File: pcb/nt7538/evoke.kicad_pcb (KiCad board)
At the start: 2 copper layers, 60 x 45 mm, 42 parts, among them J1 Conn_01x03_Male, J2 BACKLIGHT_CONN, J3 SUPP_PWR, Q1 Q_NMOS_GSD, U1 STM32F103C8Tx

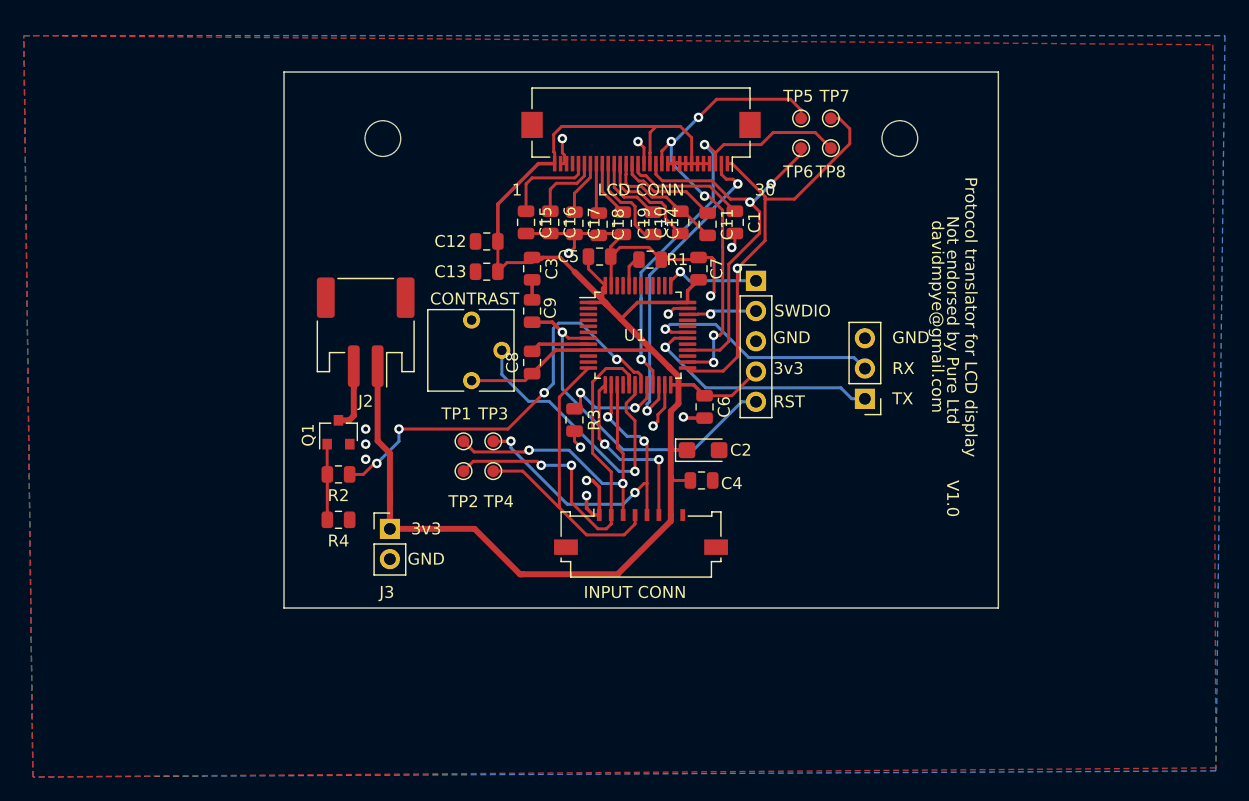
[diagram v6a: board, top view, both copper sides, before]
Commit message: Move screw holes for the nt7538 PCB, and increment PCB version number to 1.1
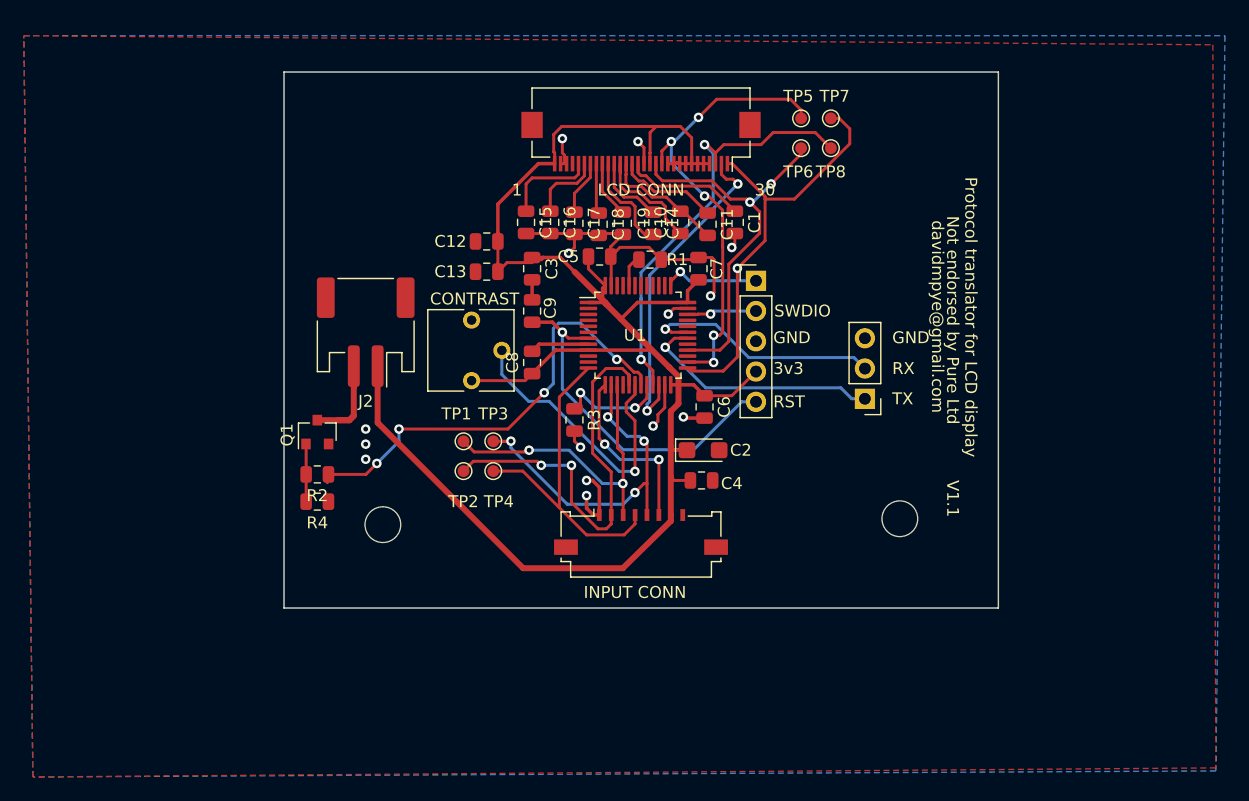
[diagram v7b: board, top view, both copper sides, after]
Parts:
- removed J3: SUPP_PWR, Connector_PinHeader_2.54mm:PinHeader_1x02_P2.54mm_Vertical
- moved REF** 32.4 mm to (83.2, 69.5)
- moved REF** 31.9 mm to (126.6, 69.0)
- moved R4 2.34 mm to (77.7, 67.6)
- moved Q1 1.78 mm to (77.7, 61.7)
- moved R2 1.78 mm to (77.7, 65.3)
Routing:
- net +3V3: track 157.2 -> 151.0 mm
- net Net-(J2-Pad2): track 5.61 -> 8.83 mm
- net LCD_BACKLIGHT_PWM: track 35.7 -> 38.4 mm
- net Net-(Q1-Pad1): track 7.06 -> 4.85 mm
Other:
- board text added: "V1.1"
- board text removed: "V1.0"
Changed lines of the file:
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@@
   (general
     (thickness 1.6)
-    (drawings 19)
-    (tracks 474)
+    (drawings 17)
+    (tracks 467)
     (zones 0)
-    (modules 42)
+    (modules 41)
     (nets 57)
   )
@@
   )
   (module MountingHole:MountingHole_3mm locked (layer F.Cu)
-    (at 126.63 37.084)
+    (at 126.63 69)
     (descr "Mounting Hole 3mm, no annular")
     (tags "mounting hole 3mm no annular")
@@
   )
   (module MountingHole:MountingHole_3mm locked (layer F.Cu)
-    (at 83.23 37.084)
+    (at 83.23 69.496)
     (descr "Mounting Hole 3mm, no annular")
     (tags "mounting hole 3mm no annular")
@@
   )
   (module Package_TO_SOT_SMD:SOT-23 (layer F.Cu)
-    (at 79.502 61.738 90)
+    (at 77.724 61.722 90)
     (descr "SOT-23, Standard")
     (tags SOT-23)
@@
   )
   (module Resistor_SMD:R_0805_2012Metric (layer F.Cu)
-    (at 79.502 65.278)
+    (at 77.724 65.278)
     (descr "Resistor SMD 0805 (2012 Metric), square (rectangular) end terminal, IPC_7351 nominal, (Body size source: https://docs.google.com/spreadsheets/d/1BsfQQcO9C6DZCsRaXUlFlo91Tg2WpOkGARC1WS5S8t0/edit?usp=sharing), generated with kicad-footprint-generator")
     (tags resistor)
@@
   )
   (module Resistor_SMD:R_0805_2012Metric (layer F.Cu)
-    (at 79.502 69.088)
+    (at 77.724 67.564)
     (descr "Resistor SMD 0805 (2012 Metric), square (rectangular) end terminal, IPC_7351 nominal, (Body size source: https://docs.google.com/spreadsheets/d/1BsfQQcO9C6DZCsRaXUlFlo91Tg2WpOkGARC1WS5S8t0/edit?usp=sharing), generated with kicad-footprint-generator")
     (tags resistor)
@@
       (net 53 "Net-(Q1-Pad1)"))
     (model ${KISYS3DMOD}/Resistor_SMD.3dshapes/R_0805_2012Metric.wrl
-      (at (xyz 0 0 0))
-      (scale (xyz 1 1 1))
-      (rotate (xyz 0 0 0))
-    )
-  )
-  (module Connector_PinHeader_2.54mm:PinHeader_1x02_P2.54mm_Vertical (layer F.Cu)
-    (at 83.82 69.85)
-    (descr "Through hole straight pin header, 1x02, 2.54mm pitch, single row")
-    (tags "Through hole pin header THT 1x02 2.54mm single row")
-    (fp_text reference J3 (at -0.254 5.334) (layer F.SilkS)
-      (effects (font (size 1 1) (thickness 0.15)))
-    )
-    (fp_text value SUPP_PWR (at 0 4.87) (layer F.Fab)
-      (effects (font (size 1 1) (thickness 0.15)))
-    )
-    (fp_line (start -0.635 -1.27) (end 1.27 -1.27) (layer F.Fab) (width 0.1))
-    (fp_line (start 1.27 -1.27) (end 1.27 3.81) (layer F.Fab) (width 0.1))
-    (fp_line (start 1.27 3.81) (end -1.27 3.81) (layer F.Fab) (width 0.1))
-    (fp_line (start -1.27 3.81) (end -1.27 -0.635) (layer F.Fab) (width 0.1))
-    (fp_line (start -1.27 -0.635) (end -0.635 -1.27) (layer F.Fab) (width 0.1))
-    (fp_line (start -1.33 3.87) (end 1.33 3.87) (layer F.SilkS) (width 0.12))
-    (fp_line (start -1.33 1.27) (end -1.33 3.87) (layer F.SilkS) (width 0.12))
-    (fp_line (start 1.33 1.27) (end 1.33 3.87) (layer F.SilkS) (width 0.12))
-    (fp_line (start -1.33 1.27) (end 1.33 1.27) (layer F.SilkS) (width 0.12))
-    (fp_line (start -1.33 0) (end -1.33 -1.33) (layer F.SilkS) (width 0.12))
-    (fp_line (start -1.33 -1.33) (end 0 -1.33) (layer F.SilkS) (width 0.12))
-    (fp_line (start -1.8 -1.8) (end -1.8 4.35) (layer F.CrtYd) (width 0.05))
-    (fp_line (start -1.8 4.35) (end 1.8 4.35) (layer F.CrtYd) (width 0.05))
-    (fp_line (start 1.8 4.35) (end 1.8 -1.8) (layer F.CrtYd) (width 0.05))
-    (fp_line (start 1.8 -1.8) (end -1.8 -1.8) (layer F.CrtYd) (width 0.05))
-    (fp_text user %R (at 0 1.27 90) (layer F.Fab)
-      (effects (font (size 1 1) (thickness 0.15)))
-    )
-    (pad 1 thru_hole rect (at 0 0) (size 1.7 1.7) (drill 1) (layers *.Cu *.Mask)
-      (net 5 +3V3))
-    (pad 2 thru_hole oval (at 0 2.54) (size 1.7 1.7) (drill 1) (layers *.Cu *.Mask)
-      (net 35 GND))
-    (model ${KISYS3DMOD}/Connector_PinHeader_2.54mm.3dshapes/PinHeader_1x02_P2.54mm_Vertical.wrl
       (at (xyz 0 0 0))
       (scale (xyz 1 1 1))
@@
     )
   )
-  (gr_text GND (at 86.868 72.39) (layer F.SilkS)
-    (effects (font (size 1 1) (thickness 0.15)))
-  )
-  (gr_text 3v3 (at 86.868 69.85) (layer F.SilkS)
-    (effects (font (size 1 1) (thickness 0.15)))
-  )
   (gr_text TX (at 125.984 58.928) (layer F.SilkS)
     (effects (font (size 1 1) (thickness 0.2)) (justify left))
@@
     (effects (font (size 1 1) (thickness 0.2)))
   )
-  (gr_text V1.0 (at 131.064 67.31 270) (layer F.SilkS)
+  (gr_text V1.1 (at 131.064 67.31 270) (layer F.SilkS)
     (effects (font (size 1 1) (thickness 0.15)))
   )
@@
   (segment (start 96.6955 47.0685) (end 95.758 47.0685) (width 0.3) (layer F.Cu) (net 5))
   (segment (start 107.402 68.686) (end 107.402 69.196002) (width 0.5) (layer F.Cu) (net 5))
-  (segment (start 82.788 62.468) (end 82.788 56.19) (width 0.5) (layer F.Cu) (net 5))
-  (segment (start 102.938002 73.66) (end 94.742 73.66) (width 0.5) (layer F.Cu) (net 5))
-  (segment (start 107.402 69.196002) (end 102.938002 73.66) (width 0.5) (layer F.Cu) (net 5))
-  (segment (start 94.996 73.66) (end 94.742 73.66) (width 0.5) (layer F.Cu) (net 5))
-  (segment (start 83.82 63.5) (end 82.788 62.468) (width 0.5) (layer F.Cu) (net 5))
-  (segment (start 83.82 68.5) (end 83.82 66.802) (width 0.5) (layer F.Cu) (net 5))
-  (segment (start 83.82 69.85) (end 83.82 68.5) (width 0.5) (layer F.Cu) (net 5))
-  (segment (start 83.82 66.802) (end 83.82 63.5) (width 0.5) (layer F.Cu) (net 5))
-  (segment (start 83.82 67.738) (end 83.82 66.802) (width 0.5) (layer F.Cu) (net 5))
-  (segment (start 90.932 69.85) (end 83.82 69.85) (width 0.5) (layer F.Cu) (net 5))
-  (segment (start 94.742 73.66) (end 90.932 69.85) (width 0.5) (layer F.Cu) (net 5))
   (segment (start 95.1715 57.404) (end 95.758 56.8175) (width 0.25) (layer F.Cu) (net 5))
   (segment (start 90.678 57.404) (end 95.1715 57.404) (width 0.25) (layer F.Cu) (net 5))
@@
   (segment (start 107.95 39.116) (end 108.152 39.188) (width 0.25) (layer F.Cu) (net 5))
   (segment (start 107.652 39.188) (end 107.95 39.116) (width 0.25) (layer F.Cu) (net 5))
+  (segment (start 82.788 60.932002) (end 95.007998 73.152) (width 0.5) (layer F.Cu) (net 5))
+  (segment (start 82.788 56.19) (end 82.788 60.932002) (width 0.5) (layer F.Cu) (net 5))
+  (segment (start 95.007998 73.152) (end 103.378 73.152) (width 0.5) (layer F.Cu) (net 5))
+  (segment (start 107.402 69.196002) (end 103.378 73.152) (width 0.5) (layer F.Cu) (net 5))
   (segment (start 112.776 43.18) (end 110.67516 41.07916) (width 0.25) (layer F.Cu) (net 6))
   (segment (start 105.305582 40.195943) (end 104.896353 40.195943) (width 0.25) (layer F.Cu) (net 6))
@@
   (segment (start 101.652 41.5325) (end 101.652 39.188) (width 0.25) (layer F.Cu) (net 52))
   (segment (start 103.378 43.2585) (end 101.652 41.5325) (width 0.25) (layer F.Cu) (net 52))
-  (segment (start 78.5645 69.088) (end 78.5645 68.388) (width 0.25) (layer F.Cu) (net 53))
-  (segment (start 78.552 65.2655) (end 78.5645 65.278) (width 0.25) (layer F.Cu) (net 53))
-  (segment (start 78.552 62.738) (end 78.552 65.2655) (width 0.25) (layer F.Cu) (net 53))
-  (segment (start 78.5645 65.978) (end 78.5645 69.088) (width 0.25) (layer F.Cu) (net 53))
-  (segment (start 78.5645 65.278) (end 78.5645 65.978) (width 0.25) (layer F.Cu) (net 53))
+  (segment (start 76.7865 62.7345) (end 76.774 62.722) (width 0.25) (layer F.Cu) (net 53))
+  (segment (start 76.7865 67.564) (end 76.7865 62.7345) (width 0.25) (layer F.Cu) (net 53))
+  (segment (start 78.552 65.2655) (end 78.5645 65.278) (width 0.25) (layer F.Cu) (net 55))
+  (segment (start 78.5645 65.278) (end 78.5645 65.978) (width 0.25) (layer F.Cu) (net 55))
   (segment (start 80.788 57.94) (end 80.788 56.19) (width 0.5) (layer F.Cu) (net 54))
   (segment (start 80.788 60.352) (end 80.788 57.94) (width 0.5) (layer F.Cu) (net 54))
   (segment (start 80.402 60.738) (end 80.788 60.352) (width 0.5) (layer F.Cu) (net 54))
   (segment (start 79.502 60.738) (end 80.402 60.738) (width 0.5) (layer F.Cu) (net 54))
+  (segment (start 80.418 60.722) (end 80.788 60.352) (width 0.5) (layer F.Cu) (net 54))
+  (segment (start 77.724 60.722) (end 80.418 60.722) (width 0.5) (layer F.Cu) (net 54))
   (via (at 102.87 55.626) (size 0.8) (drill 0.4) (layers F.Cu B.Cu) (net 55))
   (segment (start 103.24141 55.626) (end 102.87 55.626) (width 0.25) (layer F.Cu) (net 55))
@@
   (segment (start 84.582 62.500149) (end 82.72511 64.357039) (width 0.25) (layer B.Cu) (net 55))
   (segment (start 84.582 61.468) (end 84.582 62.500149) (width 0.25) (layer B.Cu) (net 55))
-  (segment (start 80.927 65.278) (end 80.4395 65.278) (width 0.25) (layer F.Cu) (net 55))
-  (segment (start 81.591002 65.278) (end 80.927 65.278) (width 0.25) (layer F.Cu) (net 55))
-  (segment (start 82.513001 64.356001) (end 81.591002 65.278) (width 0.25) (layer F.Cu) (net 55))
   (segment (start 82.724072 64.356001) (end 82.513001 64.356001) (width 0.25) (layer F.Cu) (net 55))
   (segment (start 82.72511 64.357039) (end 82.724072 64.356001) (width 0.25) (layer F.Cu) (net 55))
   (segment (start 93.726 61.468) (end 96.774 58.42) (width 0.25) (layer F.Cu) (net 55))
   (segment (start 84.582 61.468) (end 93.726 61.468) (width 0.25) (layer F.Cu) (net 55))
+  (segment (start 81.804149 65.278) (end 78.6615 65.278) (width 0.25) (layer F.Cu) (net 55))
+  (segment (start 82.72511 64.357039) (end 81.804149 65.278) (width 0.25) (layer F.Cu) (net 55))
   (zone (net 35) (net_name GND) (layer B.Cu) (hatch edge 0.508)
     (connect_pads (clearance 0.508))
